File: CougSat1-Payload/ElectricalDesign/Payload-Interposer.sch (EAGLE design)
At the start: 47 parts, among them J1 CougSat Card, J3 Interposer, J5 Germination Chamber, Q2 CSD25402Q3A, U1 TXS0102DQM, U2 TXS0102DQM, U3 TXS0102DQM, U4 BME280, U5 TLC59116F, U6 TXS0102DQM

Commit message: Made changes
requested by HMS Hendrik
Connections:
- net N$13 renamed LED_1_INT
- net N$16 renamed LED_2_INT
- net N$17 renamed LED_3_INT
- net N$18 renamed LED_4_INT
- net N$19 renamed LED-1
- net N$20 renamed LED-\2
- net N$21 renamed LED-3
- net N$22 renamed LED-4
- net N$23 renamed HEATER_SOURCE
- net N$8 renamed HEATER
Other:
- note removed: "HEATER"
- note removed: "LED 1"
- note removed: "LED 2"
- note removed: "LED 3"
- note removed: "LED 4"
- moved on the sheet: DS1, R6
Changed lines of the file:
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@@
 <?xml version="1.0" encoding="utf-8"?>
 <!DOCTYPE eagle SYSTEM "eagle.dtd">
-<eagle version="9.5.1">
+<eagle version="9.5.2">
 <drawing>
 <settings>
@@
 <text x="154.94" y="170.18" size="1.778" layer="97" align="center">CAD Note:
 U5 Decoupling</text>
-<text x="170.18" y="132.08" size="1.778" layer="95">LED 1</text>
-<text x="170.18" y="129.54" size="1.778" layer="95">LED 2</text>
-<text x="170.18" y="127" size="1.778" layer="95">LED 3</text>
-<text x="170.18" y="124.46" size="1.778" layer="95">LED 4</text>
-<text x="170.18" y="121.92" size="1.778" layer="95">HEATER</text>
 <wire x1="58.42" y1="187.96" x2="78.74" y2="187.96" width="0.1524" layer="97" style="shortdash"/>
 <wire x1="78.74" y1="187.96" x2="78.74" y2="164.592" width="0.1524" layer="97" style="shortdash"/>
@@
 <attribute name="VALUE" x="241.3" y="161.036" size="1.27" layer="96" align="center"/>
 </instance>
-<instance part="R6" gate="G$1" x="179.324" y="134.62" smashed="yes">
-<attribute name="NAME" x="180.594" y="139.7" size="1.27" layer="95" align="center-left"/>
-<attribute name="VALUE" x="180.594" y="138.176" size="1.27" layer="96" align="center-left"/>
-<attribute name="PACKAGE" x="180.594" y="135.128" size="1.27" layer="97" align="center-left"/>
-<attribute name="POWER" x="180.594" y="133.604" size="1.27" layer="97" align="center-left"/>
-<attribute name="TEMP" x="180.594" y="132.08" size="1.27" layer="97" align="center-left"/>
-<attribute name="SKU" x="180.594" y="136.652" size="1.27" layer="97" align="center-left"/>
+<instance part="R6" gate="G$1" x="179.324" y="137.16" smashed="yes">
+<attribute name="NAME" x="180.594" y="142.24" size="1.27" layer="95" align="center-left"/>
+<attribute name="VALUE" x="180.594" y="140.716" size="1.27" layer="96" align="center-left"/>
+<attribute name="PACKAGE" x="180.594" y="137.668" size="1.27" layer="97" align="center-left"/>
+<attribute name="POWER" x="180.594" y="136.144" size="1.27" layer="97" align="center-left"/>
+<attribute name="TEMP" x="180.594" y="134.62" size="1.27" layer="97" align="center-left"/>
+<attribute name="SKU" x="180.594" y="139.192" size="1.27" layer="97" align="center-left"/>
 </instance>
 <instance part="R7" gate="G$1" x="192.024" y="137.16" smashed="yes">
@@
 <attribute name="SKU" x="218.694" y="139.192" size="1.27" layer="97" align="center-left"/>
 </instance>
-<instance part="SUPPLY55" gate="G$1" x="179.324" y="149.86" smashed="yes">
-<attribute name="VALUE" x="179.324" y="153.416" size="1.27" layer="96" align="center"/>
+<instance part="SUPPLY55" gate="G$1" x="179.324" y="152.4" smashed="yes">
+<attribute name="VALUE" x="179.324" y="155.956" size="1.27" layer="96" align="center"/>
 </instance>
 <instance part="SUPPLY57" gate="G$1" x="192.024" y="152.4" smashed="yes">
@@
 </instance>
 <instance part="SUPPLY60" gate="G$1" x="241.3" y="121.92" smashed="yes"/>
-<instance part="DS1" gate="G$1" x="179.324" y="144.78" smashed="yes">
-<attribute name="NAME" x="181.864" y="149.86" size="1.27" layer="95" align="center-left"/>
-<attribute name="VALUE" x="181.864" y="148.336" size="1.27" layer="95" align="center-left"/>
-<attribute name="SKU" x="181.864" y="146.812" size="1.27" layer="95" align="center-left"/>
-<attribute name="CURRENT" x="181.864" y="143.764" size="1.27" layer="95" align="center-left"/>
-<attribute name="VF" x="181.864" y="142.24" size="1.27" layer="95" align="center-left"/>
-<attribute name="PACKAGE" x="181.864" y="145.288" size="1.27" layer="95" align="center-left"/>
+<instance part="DS1" gate="G$1" x="179.324" y="147.32" smashed="yes">
+<attribute name="NAME" x="181.864" y="152.4" size="1.27" layer="95" align="center-left"/>
+<attribute name="VALUE" x="181.864" y="150.876" size="1.27" layer="95" align="center-left"/>
+<attribute name="SKU" x="181.864" y="149.352" size="1.27" layer="95" align="center-left"/>
+<attribute name="CURRENT" x="181.864" y="146.304" size="1.27" layer="95" align="center-left"/>
+<attribute name="VF" x="181.864" y="144.78" size="1.27" layer="95" align="center-left"/>
+<attribute name="PACKAGE" x="181.864" y="147.828" size="1.27" layer="95" align="center-left"/>
 </instance>
 <instance part="DS2" gate="G$1" x="192.024" y="147.32" smashed="yes">
@@
 </segment>
 </net>
-<net name="N$8" class="0">
+<net name="HEATER" class="0">
 <segment>
 <pinref part="U5" gate="G$1" pin="!OUT0"/>
@@
 <wire x1="233.68" y1="142.24" x2="228.6" y2="142.24" width="0.1524" layer="91"/>
 <junction x="228.6" y="142.24"/>
-</segment>
-</net>
-<net name="N$13" class="0">
+<label x="170.18" y="121.92" size="1.778" layer="95"/>
+</segment>
+</net>
+<net name="LED_1_INT" class="0">
 <segment>
 <pinref part="R6" gate="G$1" pin="2"/>
-<wire x1="179.324" y1="142.24" x2="179.324" y2="139.7" width="0.1524" layer="91"/>
 <pinref part="DS1" gate="G$1" pin="C"/>
-</segment>
-</net>
-<net name="N$16" class="0">
+<wire x1="179.324" y1="144.78" x2="179.324" y2="142.24" width="0.1524" layer="91"/>
+</segment>
+</net>
+<net name="LED_2_INT" class="0">
 <segment>
 <pinref part="R7" gate="G$1" pin="2"/>
@@
 </segment>
 </net>
-<net name="N$17" class="0">
+<net name="LED_3_INT" class="0">
 <segment>
 <pinref part="R9" gate="G$1" pin="2"/>
@@
 </segment>
 </net>
-<net name="N$18" class="0">
+<net name="LED_4_INT" class="0">
 <segment>
 <pinref part="R10" gate="G$1" pin="2"/>
@@
 </segment>
 </net>
-<net name="N$19" class="0">
-<segment>
-<pinref part="R6" gate="G$1" pin="1"/>
-<pinref part="U5" gate="G$1" pin="!OUT4"/>
-<wire x1="179.324" y1="132.08" x2="170.18" y2="132.08" width="0.1524" layer="91"/>
-</segment>
-</net>
-<net name="N$20" class="0">
+<net name="LED-\2" class="0">
 <segment>
 <pinref part="R7" gate="G$1" pin="1"/>
@@
 <wire x1="192.024" y1="134.62" x2="192.024" y2="129.54" width="0.1524" layer="91"/>
 <wire x1="192.024" y1="129.54" x2="170.18" y2="129.54" width="0.1524" layer="91"/>
-</segment>
-</net>
-<net name="N$21" class="0">
+<label x="170.18" y="129.54" size="1.778" layer="95"/>
+</segment>
+</net>
+<net name="LED-3" class="0">
 <segment>
 <pinref part="R9" gate="G$1" pin="1"/>
@@
 <wire x1="204.724" y1="134.62" x2="204.724" y2="127" width="0.1524" layer="91"/>
 <wire x1="204.724" y1="127" x2="170.18" y2="127" width="0.1524" layer="91"/>
-</segment>
-</net>
-<net name="N$22" class="0">
+<label x="170.18" y="127" size="1.778" layer="95"/>
+</segment>
+</net>
+<net name="LED-4" class="0">
 <segment>
 <pinref part="R10" gate="G$1" pin="1"/>
@@
 <wire x1="217.424" y1="134.62" x2="217.424" y2="124.46" width="0.1524" layer="91"/>
 <wire x1="217.424" y1="124.46" x2="170.18" y2="124.46" width="0.1524" layer="91"/>
-</segment>
-</net>
-<net name="N$23" class="0">
+<label x="170.18" y="124.46" size="1.778" layer="95"/>
+</segment>
+</net>
+<net name="HEATER_SOURCE" class="0">
 <segment>
 <pinref part="R11" gate="G$1" pin="2"/>
 <pinref part="Q2" gate="G$1" pin="D"/>
 <wire x1="241.3" y1="132.08" x2="241.3" y2="134.62" width="0.1524" layer="91"/>
+</segment>
+</net>
+<net name="LED-1" class="0">
+<segment>
+<pinref part="U5" gate="G$1" pin="!OUT4"/>
+<pinref part="R6" gate="G$1" pin="1"/>
+<wire x1="170.18" y1="132.08" x2="179.324" y2="132.08" width="0.1524" layer="91"/>
+<wire x1="179.324" y1="132.08" x2="179.324" y2="134.62" width="0.1524" layer="91"/>
+<label x="170.18" y="132.08" size="1.778" layer="95"/>
 </segment>
 </net>
@@
 <attribute name="LENS" x="149.86" y="78.486" size="1.778" layer="97" rot="MR0" align="center"/>
 </instance>
-<instance part="SUPPLY25" gate="G$1" x="119.38" y="86.36" smashed="yes"/>
+<instance part="SUPPLY25" gate="G$1" x="116.84" y="81.28" smashed="yes"/>
 <instance part="SUPPLY26" gate="G$1" x="223.52" y="177.8" smashed="yes"/>
 <instance part="SUPPLY27" gate="G$1" x="243.84" y="175.26" smashed="yes"/>
@@
 <pinref part="B1" gate="G$1" pin="DGND"/>
 <pinref part="SUPPLY25" gate="G$1" pin="PGND"/>
-<wire x1="121.92" y1="88.9" x2="119.38" y2="88.9" width="0.1524" layer="91"/>
+<wire x1="121.92" y1="88.9" x2="116.84" y2="88.9" width="0.1524" layer="91"/>
+<wire x1="116.84" y1="88.9" x2="116.84" y2="83.82" width="0.1524" layer="91"/>
 </segment>
 <segment>
@@
 <segment>
 <pinref part="U4" gate="G$1" pin="SCK"/>
-<pinref part="R4" gate="G$1" pin="1"/>
-<wire x1="106.68" y1="147.32" x2="106.68" y2="154.94" width="0.1524" layer="91"/>
-<wire x1="86.36" y1="147.32" x2="106.68" y2="147.32" width="0.1524" layer="91"/>
 <pinref part="B2" gate="G$1" pin="RX/SCL"/>
 <wire x1="86.36" y1="20.32" x2="81.28" y2="20.32" width="0.1524" layer="91"/>
@@
 <wire x1="45.72" y1="106.68" x2="45.72" y2="134.62" width="0.1524" layer="91"/>
 <wire x1="45.72" y1="134.62" x2="86.36" y2="134.62" width="0.1524" layer="91"/>
-<wire x1="86.36" y1="134.62" x2="86.36" y2="147.32" width="0.1524" layer="91"/>
 <wire x1="86.36" y1="165.1" x2="86.36" y2="147.32" width="0.1524" layer="91"/>
+<wire x1="86.36" y1="147.32" x2="86.36" y2="134.62" width="0.1524" layer="91"/>
 <wire x1="86.36" y1="165.1" x2="83.82" y2="165.1" width="0.1524" layer="91"/>
 <junction x="45.72" y="106.68"/>
@@
 <junction x="45.72" y="83.82"/>
 <wire x1="23.0124" y1="106.68" x2="45.72" y2="106.68" width="0.1524" layer="91"/>
+<pinref part="R4" gate="G$1" pin="1"/>
+<wire x1="106.68" y1="147.32" x2="106.68" y2="154.94" width="0.1524" layer="91"/>
+<wire x1="106.68" y1="147.32" x2="86.36" y2="147.32" width="0.1524" layer="91"/>
+<junction x="86.36" y="147.32"/>
 </segment>
 <segment>
@@
 </segment>
 </net>
-<net name="N$3" class="0">
-<segment>
-<junction x="86.36" y="147.32"/>
-</segment>
-</net>

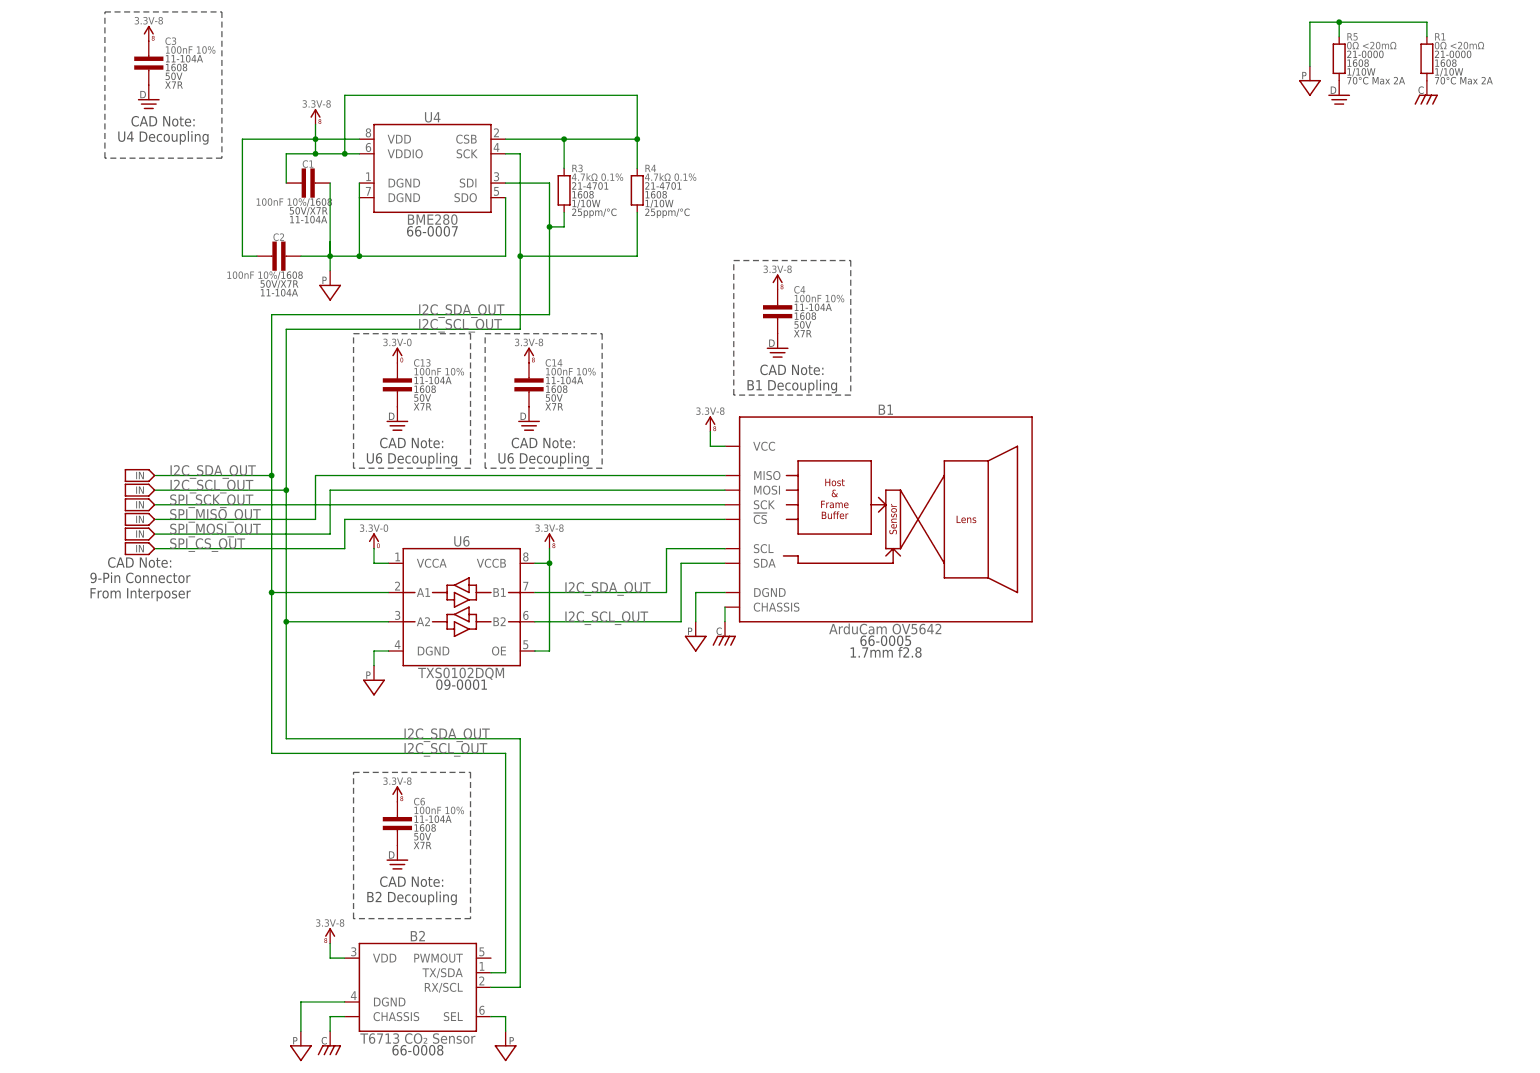
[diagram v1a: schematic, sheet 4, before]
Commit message: Updated schematic
Separated chamber components from interposer components in schematic.
Sheet 3 now has interposer components
Sheet 4 now has Chamber components
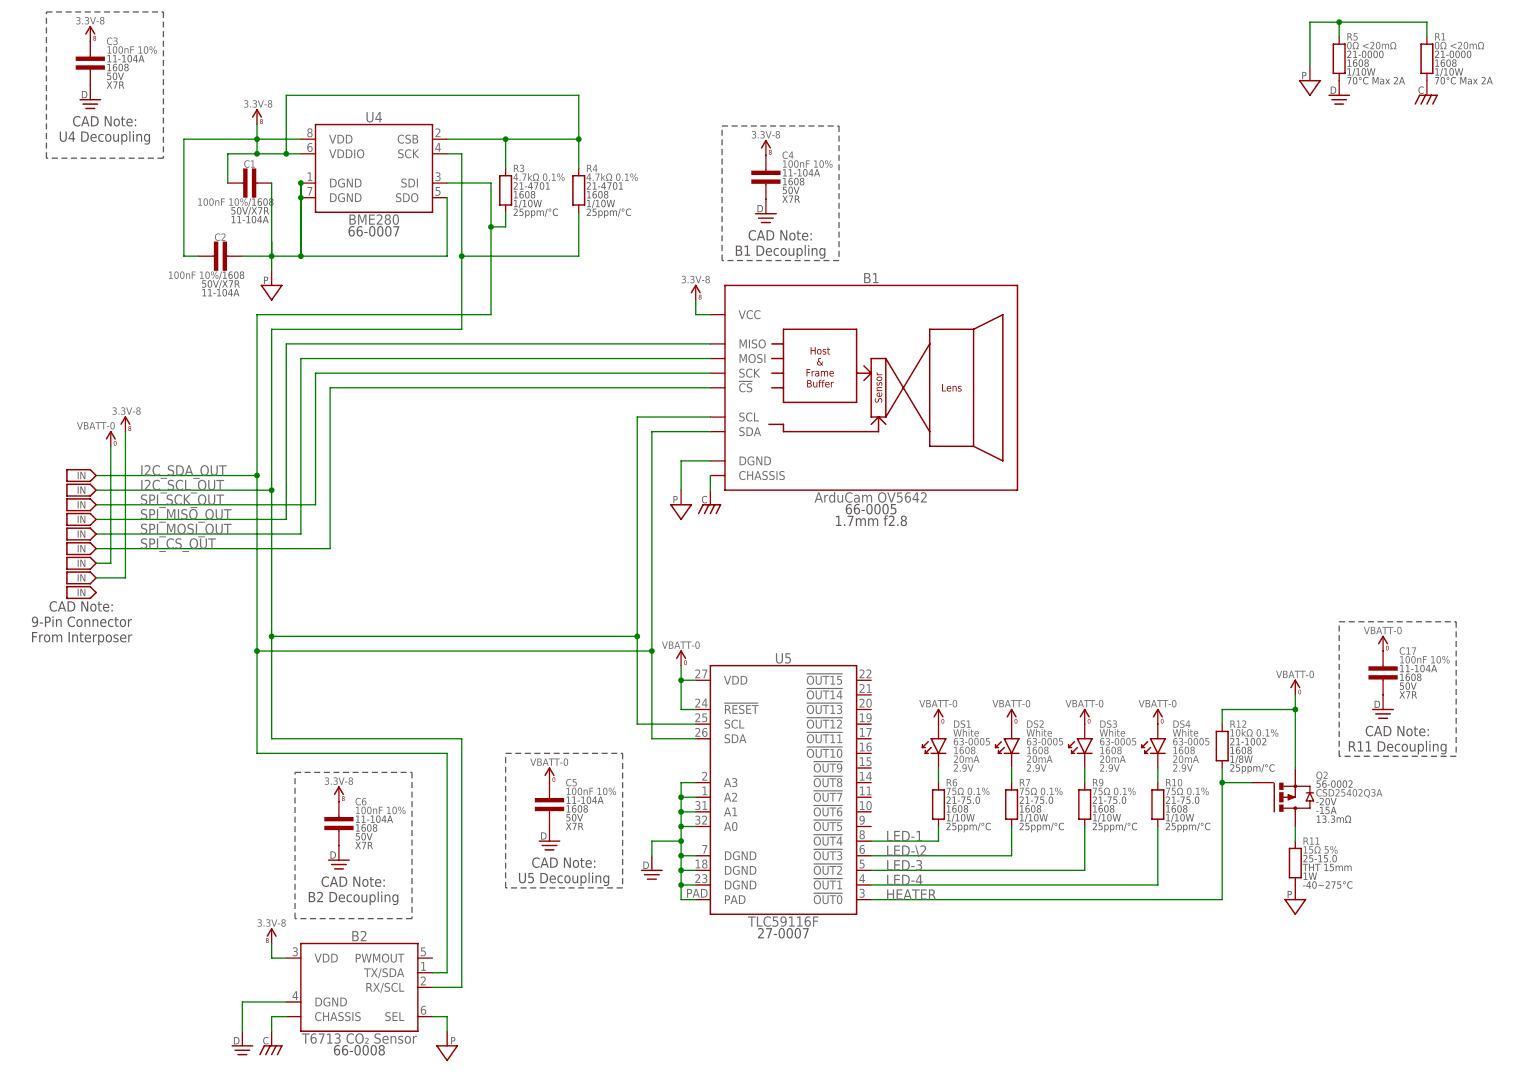
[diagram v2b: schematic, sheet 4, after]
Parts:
- removed C13, C14, C15, C16, C18, C19, C20: 100nF 10%, CougsInSpace-Capacitors:CAP-V-100NF-1608
- removed U6: TXS0102DQM, CougsInSpace-IC-Comms:LEVEL_SHIFTER-2BIT-XSON-8
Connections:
- net 3.3V_0: no longer C13.1, U6.VCCA
- net 3.3V_8: now also J5.8; no longer C14.1, U6.OE, U6.VCCB
- net DGND: now also B2.DGND, U5.PAD; no longer C13.2, C14.2, C15.2, C16.2, C18.2, C19.2, C20.2
- net I2C_SCL_OUT: now also B1.SCL, J5.2; no longer B1.SDA, J3.1, U6.A2, U6.B2
- net I2C_SDA_OUT: now also B1.SDA, J3.1, J5.1; no longer B1.SCL, U6.A1, U6.B1
- net PGND: now also J3.9, J5.9; no longer B2.DGND, J3.10, U6.DGND
- net SPI_CS_OUT: now also J5.6
- net SPI_MISO_OUT: now also J5.4
- net SPI_MOSI_OUT: now also J5.5
- net SPI_SCK_OUT: now also J5.3
- net VBATT_0: now also J5.7, U5.!RESET; no longer C15.1, C16.1, C18.1, C19.1, C20.1
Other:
- note removed: "CAD Note: DS1 Decoupling"
- note removed: "CAD Note: DS2 Decoupling"
- note removed: "CAD Note: DS3 Decoupling"
- note removed: "CAD Note: DS4 Decoupling"
- note removed: "CAD Note: DS5 Decoupling"
- note removed: "CAD Note: U6 Decoupling"
- moved on the sheet: B1, B2, C1, C2, C3, C4, C6, J3, J5, R3, R4, U4

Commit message: Made changes
As requested by Hendrik
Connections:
- net I2C_SCL_OUT renamed I2C_SCL_GERM
- net I2C_SDA_OUT renamed I2C_SDA_GERM
- net SPI_CS_OUT renamed SPI_CS_GERM
- net SPI_MISO_OUT renamed SPI_MISO_GERM
- net SPI_MOSI_OUT renamed SPI_MOSI_GERM
- net SPI_SCK_OUT renamed SPI_SCK_GERM
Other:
- note added: "CAD Note: 9-Pin Vaccuum Bulkhead"
- note removed: "9-Pin Vaccuum Bulkhead"
- note removed: "CAD Note: 9-Pin Connector From Interposer"

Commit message: Schematic Completed
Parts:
- removed C1, C2: 100nF 10%, CougsInSpace-Capacitors:CAP-H-100NF-1608
- removed C17: 100nF 10%, CougsInSpace-Capacitors:CAP-V-100NF-1608
- removed R2: 0Ω <20mΩ, CougsInSpace-Resistors:RES-V-0-1608
- added C13: 100nF 10%, CougsInSpace-Capacitors:CAP-V-100NF-1608
- added C25, C27: 10µF 10%, CougsInSpace-Capacitors:CAP-V-10UF-1608
- added C26: 1µF 10%, CougsInSpace-Capacitors:CAP-V-1UF-B-1608
- added C28: 10nF 10%, CougsInSpace-Capacitors:CAP-V-10NF-1608
- added C29: 47µF, CougsInSpace-Capacitors:CAP-POL-V-47UF-4028
- added C30: 4.7pF ±0.1, CougsInSpace-Capacitors:CAP-V-4.7PF-1608
- added L1: 4.7µH 20%, CougsInSpace-Coils:INDUCTOR-H-4.7UH-7575
- added Q1: CSD25402Q3A, CougsInSpace-DiscreteSemi:MOSFET-P-SON-3333
- added R13, R14, R17, R18, R19, R20: 0Ω <20mΩ, CougsInSpace-Resistors:RES-V-0-1608
- added R15: 100kΩ 0.1%, CougsInSpace-Resistors:RES-V-100K-1608
- added R16: 10kΩ 0.1%, CougsInSpace-Resistors:RES-V-10K-1608
- added R8: 1MΩ 1%, CougsInSpace-Resistors:RES-V-1M-1608
- added TP4, TP5, TP6, TP7: TEST_POINT-THT-1.0, CougsInSpace-Connectors:TEST_POINT-THT-1.0
- added U14: TPS61220, CougsInSpace-IC-Power:TPS61220
- added U15: TPS73250, CougsInSpace-IC-Power:LDO-FB-5.0-SOT23-5
- R10, R6, R7, R9: value 75Ω 0.1% -> 30kΩ 1%; device CougsInSpace-Resistors:RES-V-75R-1608 -> CougsInSpace-Resistors:RES-V-30K-1608
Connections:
- net LED-\2 renamed LED-2
- removed net 3.3V_7: J1POWER.PR_3.3V-7
- new net 5.0V: B2.VDD, C25.1, TP4.1, U15.OUT
- new net BOOST_FB: C30.2, R13.1, R14.2, U14.FB
- new net BOOST_FB-HIGH: R13.2, R8.1
- new net BOOST_FB-LOW: R14.1, R15.2
- new net BOOST_IN: L1.2, U14.SW
- new net BOOST_OUT: C26.1, C29.A, C30.1, R8.2, U14.VOUT, U15.EN, U15.IN
- new net CAMERA_POWER: J3.9, J5.9, Q1.G, R16.1
- new net CAMERA_VCC: B1.VCC, Q1.D
- new net CAMER_POWER: J1GPIO.GPIO-7
- new net REG_FB: C28.1, U15.FB
- net 3.3V_8: now also C27.1, L1.1, Q1.S, R16.2, TP6.1, U14.EN, U14.VIN; no longer B1.VCC, B2.VDD, C1.1, C2.1
- net CHASSIS: now also R17.1, R19.1; no longer R2.1
- net DGND: now also B2.SEL, R18.1, R20.1, U4.DGND@1, U4.DGND@2, U4.SDO; no longer C17.2
- net PGND: now also C13.2, C25.2, C26.2, C27.2, C28.2, C29.C, J3.10, J5.10, R15.1, R17.2, R18.2, R19.2, R20.2, TP5.1, TP7.1, U14.PGND, U15.PGND; no longer B2.SEL, C1.2, C2.2, J3.9, J5.9, R2.2, U4.DGND@1, U4.DGND@2, U4.SDO
- net VBATT_0: now also C13.1; no longer C17.1, J3.7, J5.7
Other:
- note added: "3C4>"
- note added: "3D2>"
- note added: "4A3>"
- note added: ">4B2"
- note added: "Note: 500mV"

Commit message: made appropriate changes
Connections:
- net HEATER renamed !HEATER
- removed net CAMERA_POWER: J3.9, J5.9, Q1.G, R16.1
- removed net CAMER_POWER: J1GPIO.GPIO-7
- new net !CAMERA_POWER: J1GPIO.GPIO-7, J3.9, J5.9, Q1.G, R16.1
- new net N$1: U5.!RESET, U5.VDD
- net 3.3V_8: now also C13.1, C5.1, DS1.A, DS2.A, DS3.A, DS4.A, Q2.S, R12.2
- net DGND: now also U1.DGND, U2.DGND, U3.DGND
- net PGND: no longer U1.DGND, U2.DGND, U3.DGND
- net VBATT_0: no longer C13.1, C5.1, DS1.A, DS2.A, DS3.A, DS4.A, Q2.S, R12.2, U5.!RESET, U5.VDD
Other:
- note added: "CAD NOTE: PLACED IN CHAMBER"
- moved on the sheet: C13, C6, R10, R12, R6, R7, R9
